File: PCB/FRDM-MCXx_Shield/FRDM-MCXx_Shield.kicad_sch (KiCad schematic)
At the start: 14 parts, among them J2 Conn_01x04_Pin, J3 Conn_01x04_Pin, J4 Conn_01x03_Pin, J5 Conn_01x04_Pin, U1 M95010-RMN6TP

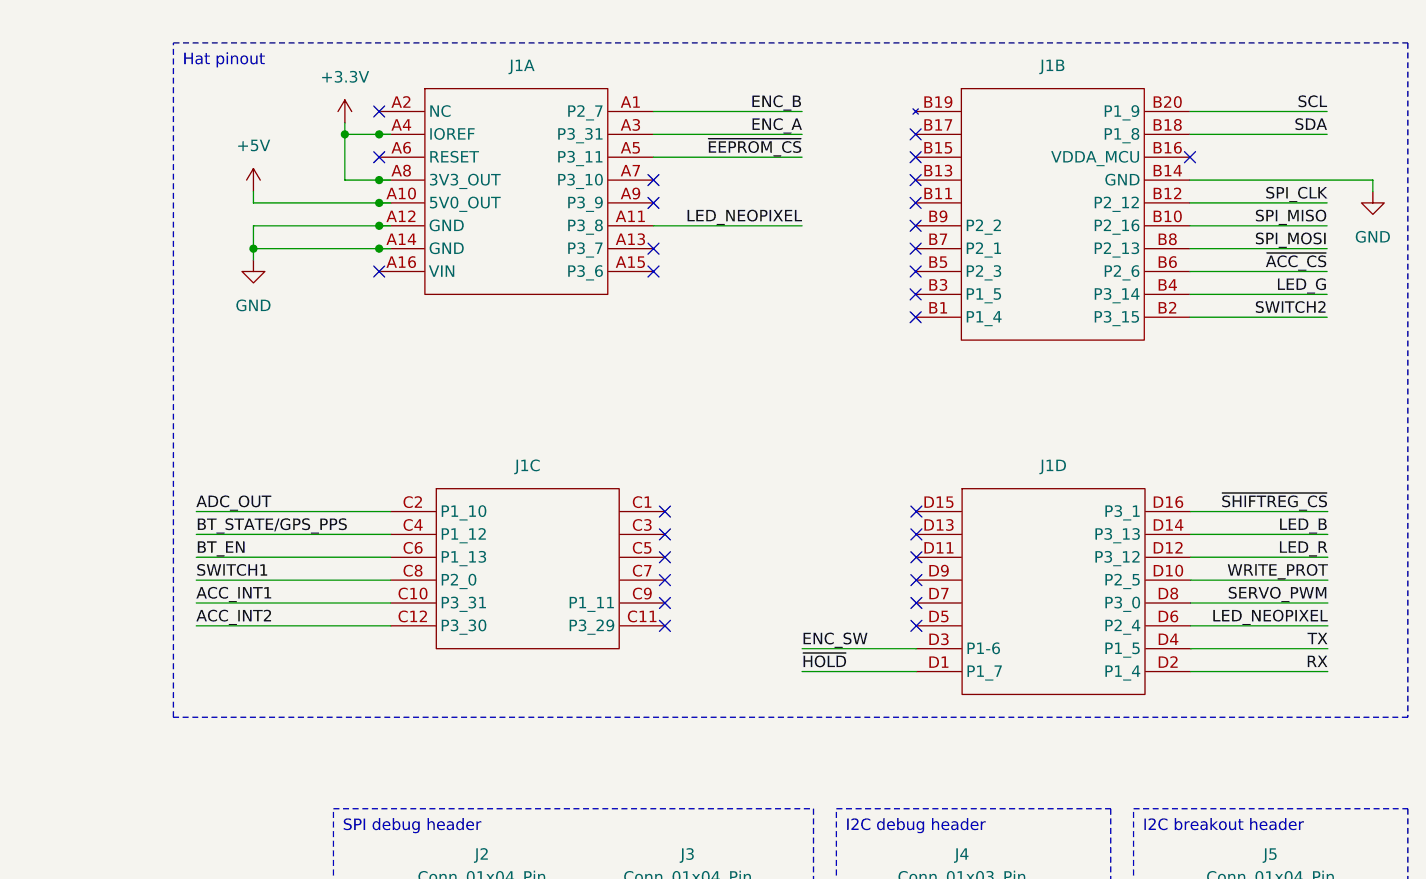
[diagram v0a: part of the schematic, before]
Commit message: Updated trace spacing and pinout
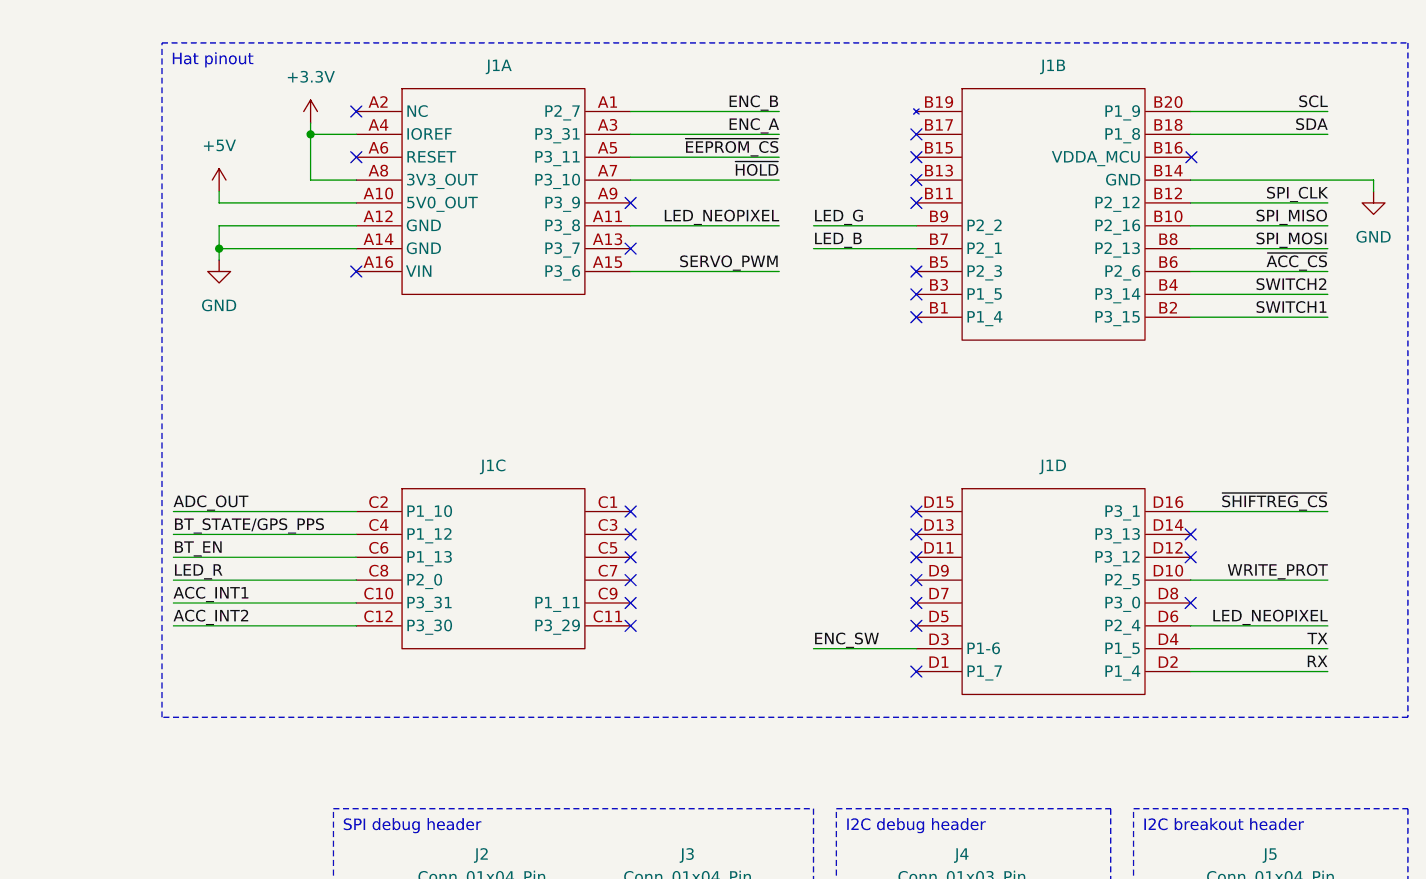
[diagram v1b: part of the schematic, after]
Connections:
- net LED_B: now also J1.B7 (P2_1); no longer J1.D14 (P3_13)
- net LED_G: now also J1.B9 (P2_2); no longer J1.B4 (P3_14)
- net LED_R: now also J1.C8 (P2_0); no longer J1.D12 (P3_12)
- net SERVO_PWM: now also J1.A15 (P3_6); no longer J1.D8 (P3_0)
- net SWITCH1: now also J1.B2 (P3_15); no longer J1.C8 (P2_0)
- net SWITCH2: now also J1.B4 (P3_14); no longer J1.B2 (P3_15)
- net ~{HOLD}: now also J1.A7 (P3_10); no longer J1.D1 (P1_7)
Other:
- moved on the sheet: J1A, J1C

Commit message: Updated V2.0
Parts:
- removed C7: 100nF, Capacitor_SMD:C_0603_1608Metric_Pad1.08x0.95mm_HandSolder, symbol Device:C
- removed D1: RED, LED_SMD:LED_0603_1608Metric_Pad1.05x0.95mm_HandSolder, symbol Device:LED
- removed D2: GREEN, LED_SMD:LED_0603_1608Metric_Pad1.05x0.95mm_HandSolder, symbol Device:LED
- removed J1: ~, User:MCX-A153_Shield_Template, symbol User:MCX-A153_Shield_Template
- removed J2, J3, J5: Conn_01x04_Pin, Connector_PinSocket_2.54mm:PinSocket_1x04_P2.54mm_Vertical, symbol Connector:Conn_01x04_Socket
- removed J4: Conn_01x03_Pin, Connector_PinSocket_2.54mm:PinSocket_1x03_P2.54mm_Vertical, symbol Connector:Conn_01x03_Socket
- removed R2 (x2): 10k, Resistor_SMD:R_0603_1608Metric_Pad0.98x0.95mm_HandSolder, symbol Device:R
- removed R2: 680, Resistor_SMD:R_0603_1608Metric_Pad0.98x0.95mm_HandSolder, symbol Device:R
- removed R2: 430, Resistor_SMD:R_0603_1608Metric_Pad0.98x0.95mm_HandSolder, symbol Device:R
- removed RN2: 4.7k, Resistor_SMD:R_Array_Convex_4x0603, symbol Device:R_Pack04_Split
- removed U1: M95010-RMN6TP, SOIC127P600X175-8N, symbol SamacSys_Parts:M95010-RMN6TP
- added J1, J4: Conn_02x08_Odd_Even, Connector_PinHeader_2.54mm:PinHeader_2x08_P2.54mm_Vertical, symbol Connector_Generic:Conn_02x08_Odd_Even
- added J2: Conn_02x06_Odd_Even, Connector_PinHeader_2.54mm:PinHeader_2x06_P2.54mm_Vertical, symbol Connector_Generic:Conn_02x06_Odd_Even
- added J3: Conn_02x10_Odd_Even, Connector_PinHeader_2.54mm:PinHeader_2x10_P2.54mm_Vertical, symbol Connector_Generic:Conn_02x10_Odd_Even
- added RN5: 4.7k, Resistor_SMD:R_Array_Convex_4x0603, symbol Device:R_Pack04_Split
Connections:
- net +3.3V: now also J4.10 (Pin_10), J4.14 (Pin_14), RN5.5 (R4.2), RN5.6 (R3.2)
- net +5V: now also J4.8 (Pin_8)
- net ADC_OUT: now also J2.12 (Pin_12)
- net ENC_A: now also J4.3 (Pin_3)
- net ENC_B: now also J4.1 (Pin_1)
- net ENC_SW: now also J1.3 (Pin_3)
- net GND: now also J3.14 (Pin_14), J4.4 (Pin_4), J4.6 (Pin_6)
- net LED_NEOPIXEL: now also J1.6 (Pin_6), J4.11 (Pin_11)
- net SCL: now also J3.20 (Pin_20), RN5.4 (R4.1)
- net SDA: now also J3.18 (Pin_18), RN5.3 (R3.1)
- net SERVO_PWM: now also J4.15 (Pin_15)
- net SPI_CLK: now also J3.12 (Pin_12)
- net SPI_MISO: now also J3.10 (Pin_10)
- net SPI_MOSI: now also J3.8 (Pin_8)
- net WRITE_PROT: now also J1.10 (Pin_10)
- net ~{EEPROM_CS}: now also J4.5 (Pin_5)
- net ~{SHIFTREG_CS}: now also J3.6 (Pin_6)
- new net ~{SHIFTREG_RST}: J1.16 (Pin_16)
- no-connect marks 29 -> 42
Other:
- sheet Actuators renamed Sensors & actuators
- sheet Sensors renamed Debug
- sheet Debug: file Sensors.kicad_sch -> Debug.kicad_sch
- sheet Debug ports: added ENC_A, ENC_B, ENC_SW, LED_NEOPIXEL, SCL, SDA, SERVO_PWM, WRITE_PROT, ~{EEPROM_CS}, ~{SHIFTREG_CS}, ~{SHIFTREG_RST}; removed ACC_INT1, ACC_INT2, BT_EN, BT_STATE/GPS_PPS, RX, TX, ~{ACC_CS}
- sheet HMI ports: added SPI_CLK, SPI_MISO, SPI_MOSI, ~{SHIFTREG_CS}, ~{SHIFTREG_RST}; removed LED_B, LED_G, LED_R, SWITCH1, SWITCH2
- sheet Sensors & actuators: file Actuators.kicad_sch -> Sensors_and_actuators.kicad_sch
- sheet Sensors & actuators ports: added ADC_OUT, WRITE_PROT, ~{EEPROM_CS}; removed ~{SHIFTREG_CS}

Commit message: Updated PCB
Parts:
- removed RN5: 4.7k, Resistor_SMD:R_Array_Convex_4x0603, symbol Device:R_Pack04_Split
- added RN1: 4.7k, Resistor_SMD:R_Array_Convex_4x1206, symbol Device:R_Pack04_Split
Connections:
- net +3.3V: now also J4.4 (Pin_4), J4.8 (Pin_8), RN1.7 (R2.2), RN1.8 (R1.2); no longer J4.10 (Pin_10), J4.14 (Pin_14)
- net +5V: now also J4.10 (Pin_10); no longer J4.8 (Pin_8)
- net ADC_OUT: now also J2.2 (Pin_2); no longer J2.12 (Pin_12)
- net GND: now also J4.12 (Pin_12), J4.14 (Pin_14); no longer J4.4 (Pin_4), J4.6 (Pin_6)
- net LED_NEOPIXEL: no longer J1.6 (Pin_6)
- net SCL: now also RN1.2 (R2.1)
- net SDA: now also RN1.1 (R1.1)
- net SERVO_PWM: now also J1.14 (Pin_14); no longer J4.15 (Pin_15)
- no-connect marks 42 -> 43
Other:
- moved on the sheet: J1, J3

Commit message: Committed latest changes
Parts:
- added H1, H2: MountingHole, MountingHole:MountingHole_2.2mm_M2, symbol Mechanical:MountingHole
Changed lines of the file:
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@@
 	(title_block
 		(title "Main")
-		(date "2024-04-27")
+		(date "2024-04-28")
 		(rev "V2.0")
 		(company "HAN")
@@
 		)
 	)
+	(text_box "Mounting holes screen bracket, M2.2"
+		(exclude_from_sim no)
+		(at 135.89 161.29 0)
+		(size 30.48 31.75)
+		(stroke
+			(width 0)
+			(type dash)
+		)
+		(fill
+			(type none)
+		)
+		(effects
+			(font
+				(size 1.27 1.27)
+			)
+			(justify left top)
+		)
+	)
 	(label "LED_NEOPIXEL"
 		(at 68.58 109.22 180)
@@
 					(unit 1)
 				)
+			)
+		)
+	)
+	(symbol
+		(lib_id "Mechanical:MountingHole")
+		(at 144.78 185.42 0)
+		(unit 1)
+		(exclude_from_sim yes)
+		(in_bom no)
+		(on_board yes)
+		(dnp no)
+		(fields_autoplaced yes)
+		(property "Reference" "H2"
+			(at 147.32 184.1499 0)
+			(effects
+				(font
+					(size 1.27 1.27)
+				)
+				(justify left)
+			)
+		)
+		(property "Value" "MountingHole"
+			(at 147.32 186.6899 0)
+			(effects
+				(font
+					(size 1.27 1.27)
+				)
+				(justify left)
+			)
+		)
+		(property "Footprint" "MountingHole:MountingHole_2.2mm_M2"
+			(at 144.78 185.42 0)
+			(effects
+				(font
+					(size 1.27 1.27)
+				)
+				(hide yes)
+			)
+		)
+		(property "Datasheet" "~"
+			(at 144.78 185.42 0)
+			(effects
+				(font
+					(size 1.27 1.27)
+				)
+				(hide yes)
+			)
+		)
+		(property "Description" "Mounting Hole without connection"
+			(at 144.78 185.42 0)
+			(effects
+				(font
+					(size 1.27 1.27)
+				)
+				(hide yes)
+			)
+		)
+		(instances
+			(project "FRDM-MCXx_Shield"
+				(path "/bffc27af-f9e0-4cc8-b5dc-88d2faf26a17"
+					(reference "H2")
+					(unit 1)
+				)
+			)
+		)
+	)
+	(symbol
+		(lib_id "Mechanical:MountingHole")
+		(at 144.78 170.18 0)
+		(unit 1)
+		(exclude_from_sim yes)
+		(in_bom no)
+		(on_board yes)
+		(dnp no)
+		(fields_autoplaced yes)
+		(property "Reference" "H1"
+			(at 147.32 168.9099 0)
+			(effects
+				(font
+					(size 1.27 1.27)
+				)
+				(justify left)
+			)
+		)
+		(property "Value" "MountingHole"
+			(at 147.32 171.4499 0)
+			(effects
+				(font
+					(size 1.27 1.27)
+				)
+				(justify left)
+			)
+		)
+		(property "Footprint" "MountingHole:MountingHole_2.2mm_M2"
+			(at 144.78 170.18 0)
+			(effects
+				(font
+					(size 1.27 1.27)
+				)
+				(hide yes)
+			)
+		)
+		(property "Datasheet" "~"
+			(at 144.78 170.18 0)
+			(effects
+				(font
+					(size 1.27 1.27)
+				)
+				(hide yes)
+			)
+		)
+		(property "Description" "Mounting Hole without connection"
+			(at 144.78 170.18 0)
+			(effects
+				(font
+					(size 1.27 1.27)
+				)
+				(hide yes)
+			)
+		)
+		(instances
+			(project "FRDM-MCXx_Shield"
+				(path "/bffc27af-f9e0-4cc8-b5dc-88d2faf26a17"
+					(reference "H1")
+					(unit 1)
+				)

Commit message: Fixed labeling
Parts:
- added REF1: WEEE-Logo_4.2x6mm_SilkScreen, Symbol:WEEE-Logo_4.2x6mm_SilkScreen, symbol Graphic:SYM_ESD_Small
- added REF2: MountingHole, Symbol:ESD-Logo_6.6x6mm_SilkScreen, symbol Mechanical:MountingHole
- added REF3: ~, clipboard:5e83e988-b69c-43c0-b382-9b895c3e7185, symbol Mechanical:MountingHole
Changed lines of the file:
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@@
+		)
+	)
+	(text_box "Symbols"
+		(exclude_from_sim no)
+		(at 179.07 119.38 0)
+		(size 48.26 31.75)
+		(stroke
+			(width 0)
+			(type dash)
+		)
+		(fill
+			(type none)
+		)
+		(effects
+			(font
+				(size 1.27 1.27)
+			)
+			(justify left top)
 		)
 	)
@@
 				(path "/bffc27af-f9e0-4cc8-b5dc-88d2faf26a17"
 					(reference "#PWR02")
+					(unit 1)
+				)
+			)
+		)
+	)
+	(symbol
+		(lib_id "Graphic:SYM_ESD_Small")
+		(at 194.31 129.54 0)
+		(unit 1)
+		(exclude_from_sim no)
+		(in_bom no)
+		(on_board no)
+		(dnp no)
+		(fields_autoplaced yes)
+		(property "Reference" "REF1"
+			(at 194.31 125.984 0)
+			(effects
+				(font
+					(size 1.27 1.27)
+				)
+				(hide yes)
+			)
+		)
+		(property "Value" "WEEE-Logo_4.2x6mm_SilkScreen"
+			(at 194.31 132.715 0)
+			(effects
+				(font
+					(size 1.27 1.27)
+				)
+				(hide yes)
+			)
+		)
+		(property "Footprint" "Symbol:WEEE-Logo_4.2x6mm_SilkScreen"
+			(at 194.31 129.286 0)
+			(effects
+				(font
+					(size 1.27 1.27)
+				)
+				(hide yes)
+			)
+		)
+		(property "Datasheet" "~"
+			(at 194.31 129.286 0)
+			(effects
+				(font
+					(size 1.27 1.27)
+				)
+				(hide yes)
+			)
+		)
+		(property "Description" ""
+			(at 194.31 129.54 0)
+			(effects
+				(font
+					(size 1.27 1.27)
+				)
+				(hide yes)
+			)
+		)
+		(instances
+			(project "FRDM-MCXx_Shield"
+				(path "/bffc27af-f9e0-4cc8-b5dc-88d2faf26a17"
+					(reference "REF1")
 					(unit 1)
 				)
@@
 	)
 	(symbol
+		(lib_id "Mechanical:MountingHole")
+		(at 194.31 142.24 0)
+		(unit 1)
+		(exclude_from_sim yes)
+		(in_bom no)
+		(on_board yes)
+		(dnp no)
+		(fields_autoplaced yes)
+		(property "Reference" "REF2"
+			(at 196.85 140.9699 0)
+			(effects
+				(font
+					(size 1.27 1.27)
+				)
+				(justify left)
+			)
+		)
+		(property "Value" "MountingHole"
+			(at 196.85 143.5099 0)
+			(effects
+				(font
+					(size 1.27 1.27)
+				)
+				(justify left)
+				(hide yes)
+			)
+		)
+		(property "Footprint" "Symbol:ESD-Logo_6.6x6mm_SilkScreen"
+			(at 194.31 142.24 0)
+			(effects
+				(font
+					(size 1.27 1.27)
+				)
+				(hide yes)
+			)
+		)
+		(property "Datasheet" "~"
+			(at 194.31 142.24 0)
+			(effects
+				(font
+					(size 1.27 1.27)
+				)
+				(hide yes)
+			)
+		)
+		(property "Description" "Mounting Hole without connection"
+			(at 194.31 142.24 0)
+			(effects
+				(font
+					(size 1.27 1.27)
+				)
+				(hide yes)
+			)
+		)
+		(instances
+			(project "FRDM-MCXx_Shield"
+				(path "/bffc27af-f9e0-4cc8-b5dc-88d2faf26a17"
+					(reference "REF2")
+					(unit 1)
+				)
+			)
+		)
+	)
+	(symbol
 		(lib_id "Connector_Generic:Conn_02x06_Odd_Even")
 		(at 242.57 44.45 0)
@@
 					(unit 1)
 				)
+			)
+		)
+	)
+	(symbol
+		(lib_id "Mechanical:MountingHole")
+		(at 213.36 142.24 0)
+		(unit 1)
+		(exclude_from_sim yes)
+		(in_bom no)
+		(on_board yes)
+		(dnp no)
+		(fields_autoplaced yes)
+		(property "Reference" "REF3"
+			(at 215.9 140.9699 0)
+			(effects
+				(font
+					(size 1.27 1.27)
+				)
+				(justify left)
+			)
+		)
+		(property "Value" "~"
+			(at 215.9 143.5099 0)
+			(effects
+				(font
+					(size 1.27 1.27)
+				)
+				(justify left)
+				(hide yes)
+			)
+		)
+		(property "Footprint" "clipboard:5e83e988-b69c-43c0-b382-9b895c3e7185"
+			(at 213.36 142.24 0)
+			(effects
+				(font
+					(size 1.27 1.27)
+				)
+				(hide yes)
+			)
+		)
+		(property "Datasheet" "~"
+			(at 213.36 142.24 0)
+			(effects
+				(font
+					(size 1.27 1.27)
+				)
+				(hide yes)
+			)
+		)
+		(property "Description" ""
+			(at 213.36 142.24 0)
+			(effects
+				(font
+					(size 1.27 1.27)
+				)
+				(hide yes)
+			)
+		)
+		(instances
+			(project "FRDM-MCXx_Shield"
+				(path "/bffc27af-f9e0-4cc8-b5dc-88d2faf26a17"
+					(reference "REF3")
+					(unit 1)
+				)
